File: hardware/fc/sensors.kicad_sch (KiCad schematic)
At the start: 7 parts, among them U6 ICM-40609-D, U7 BMP581

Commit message: fc: delete barometer; finalise schematic
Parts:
- removed C22, C23: 0.1uF, symbol Device:C_Small
- removed U7: BMP581, QFN10_BMP581_BOS, symbol BMP581:BMP581
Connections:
- net V_1V8 renamed V_IMU
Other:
- note removed: "Barometer"
- title: IMU; Barometer -> IMU
- moved on the sheet: C19, C20, C21, U6

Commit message: fc: add footprints
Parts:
- C19, C20: footprint (none) -> Stratus:C_0402
- C21: value 2.2uF -> 4.7uF; footprint (none) -> Stratus:C_0402
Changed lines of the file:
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@@
 			)
 		)
-		(property "Value" "2.2uF"
+		(property "Value" "4.7uF"
 			(at 138.43 124.4662 0)
 			(show_name no)
@@
 			)
 		)
-		(property "Footprint" ""
+		(property "Footprint" "Stratus:C_0402"
 			(at 140.97 123.19 0)
 			(hide yes)
@@
 			)
 		)
-		(property "Footprint" ""
+		(property "Footprint" "Stratus:C_0402"
 			(at 130.81 123.19 0)
 			(hide yes)
@@
 			)
 		)
-		(property "Footprint" ""
+		(property "Footprint" "Stratus:C_0402"
 			(at 120.65 123.19 0)
 			(hide yes)

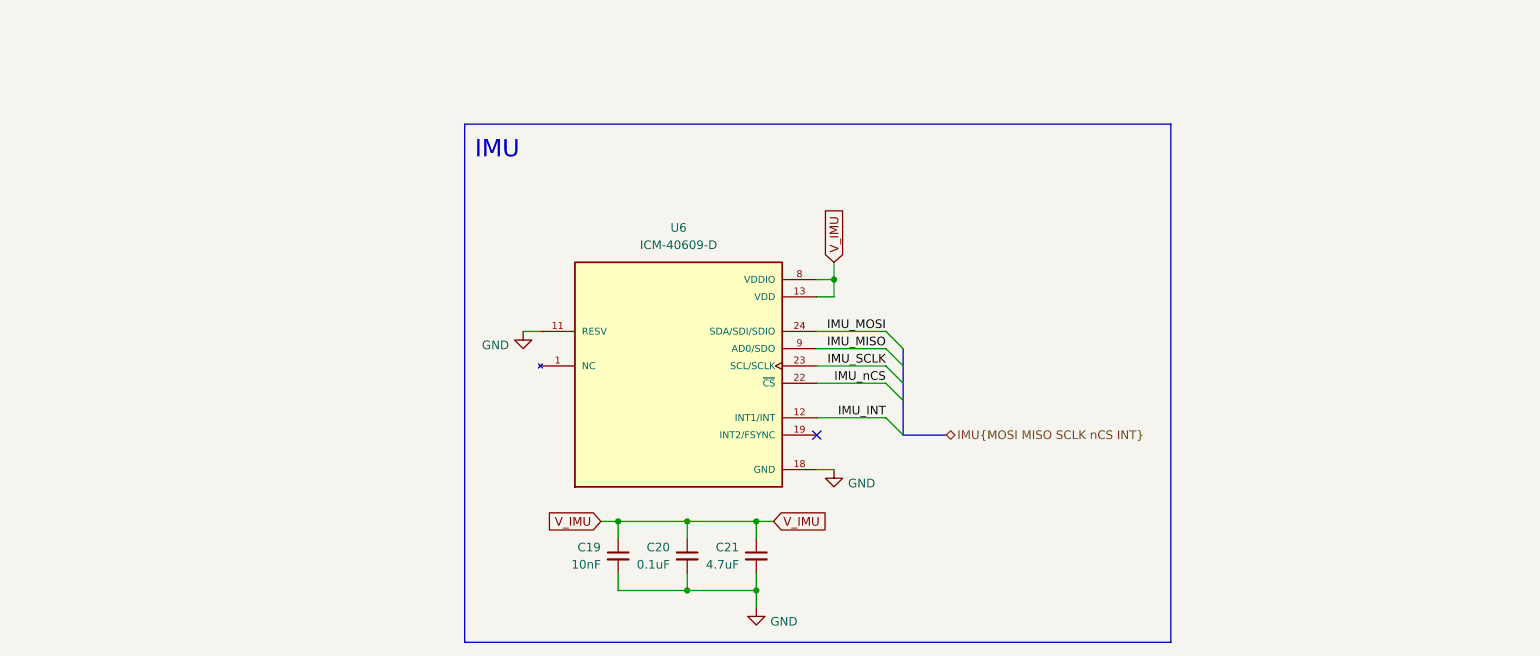
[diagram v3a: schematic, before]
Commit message: fc: fix peripherals
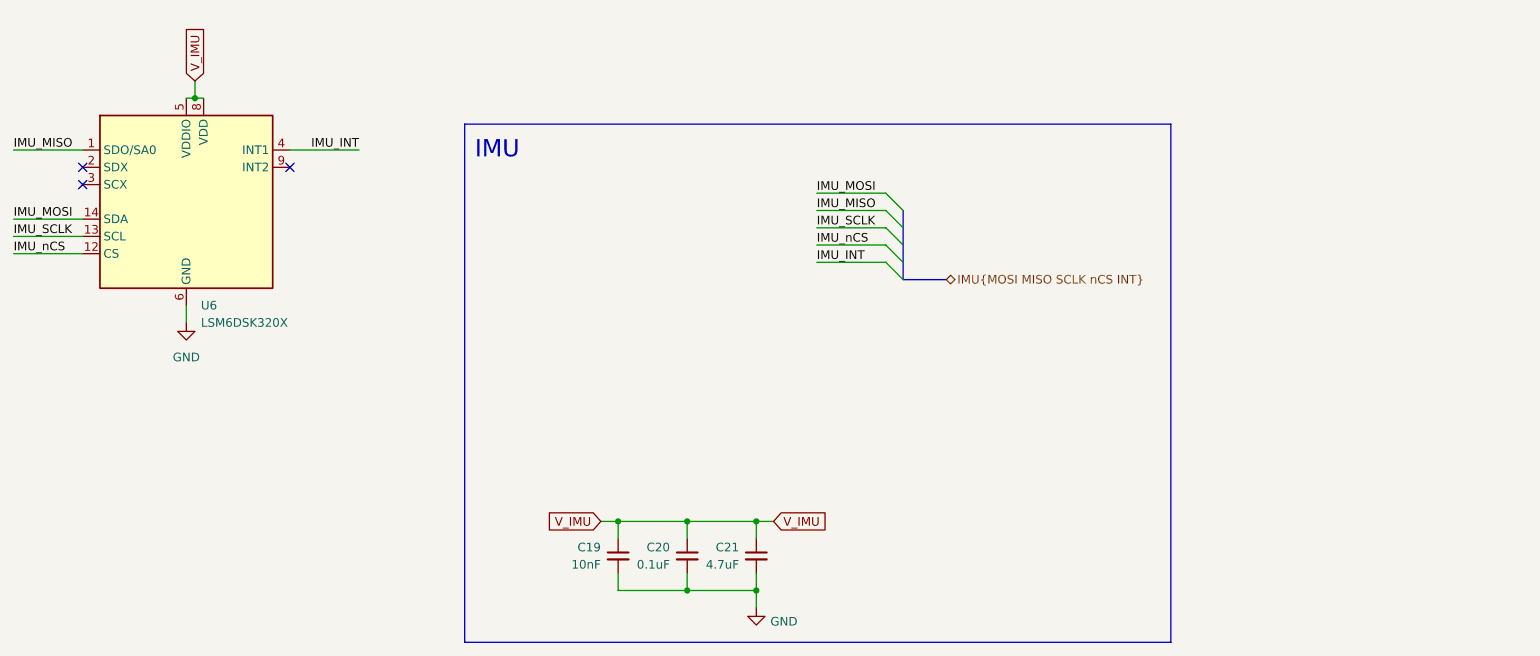
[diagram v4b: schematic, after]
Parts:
- removed U6: ICM-40609-D, ICM-40609-D:XDCR_ICM-40609-D, symbol ICM-40609-D:ICM-40609-D
- added U6: LSM6DSK320X, Package_LGA:LGA-14_3x2.5mm_P0.5mm_LayoutBorder3x4y, symbol Sensor_Motion:LSM6DS3
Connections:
- net GND: now also U6.6 (GND), U6.7 (GND)
- net IMU_INT: now also U6.4 (INT1)
- net IMU_MISO: now also U6.1 (SDO/SA0)
- net IMU_MOSI: now also U6.14 (SDA)
- net IMU_SCLK: now also U6.13 (SCL)
- net IMU_nCS: now also U6.12 (CS)
- net V_IMU: now also U6.5 (VDDIO), U6.8 (VDD)
- no-connect marks 1 -> 3
